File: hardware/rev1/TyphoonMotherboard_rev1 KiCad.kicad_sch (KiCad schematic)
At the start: 74 parts, among them J1 Conn_02x04_Odd_Even, J2 Conn_01x04_Pin, J3 UJ20-C-H-C-4-SMT-TR, J5 Conn_01x02_Pin, J6 Conn_01x02_Pin, J7 Conn_01x04_Pin, SW1 SW_Push, SW2 SW_Push, SW3 SW_Push, U1 USBLC6-2SC6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

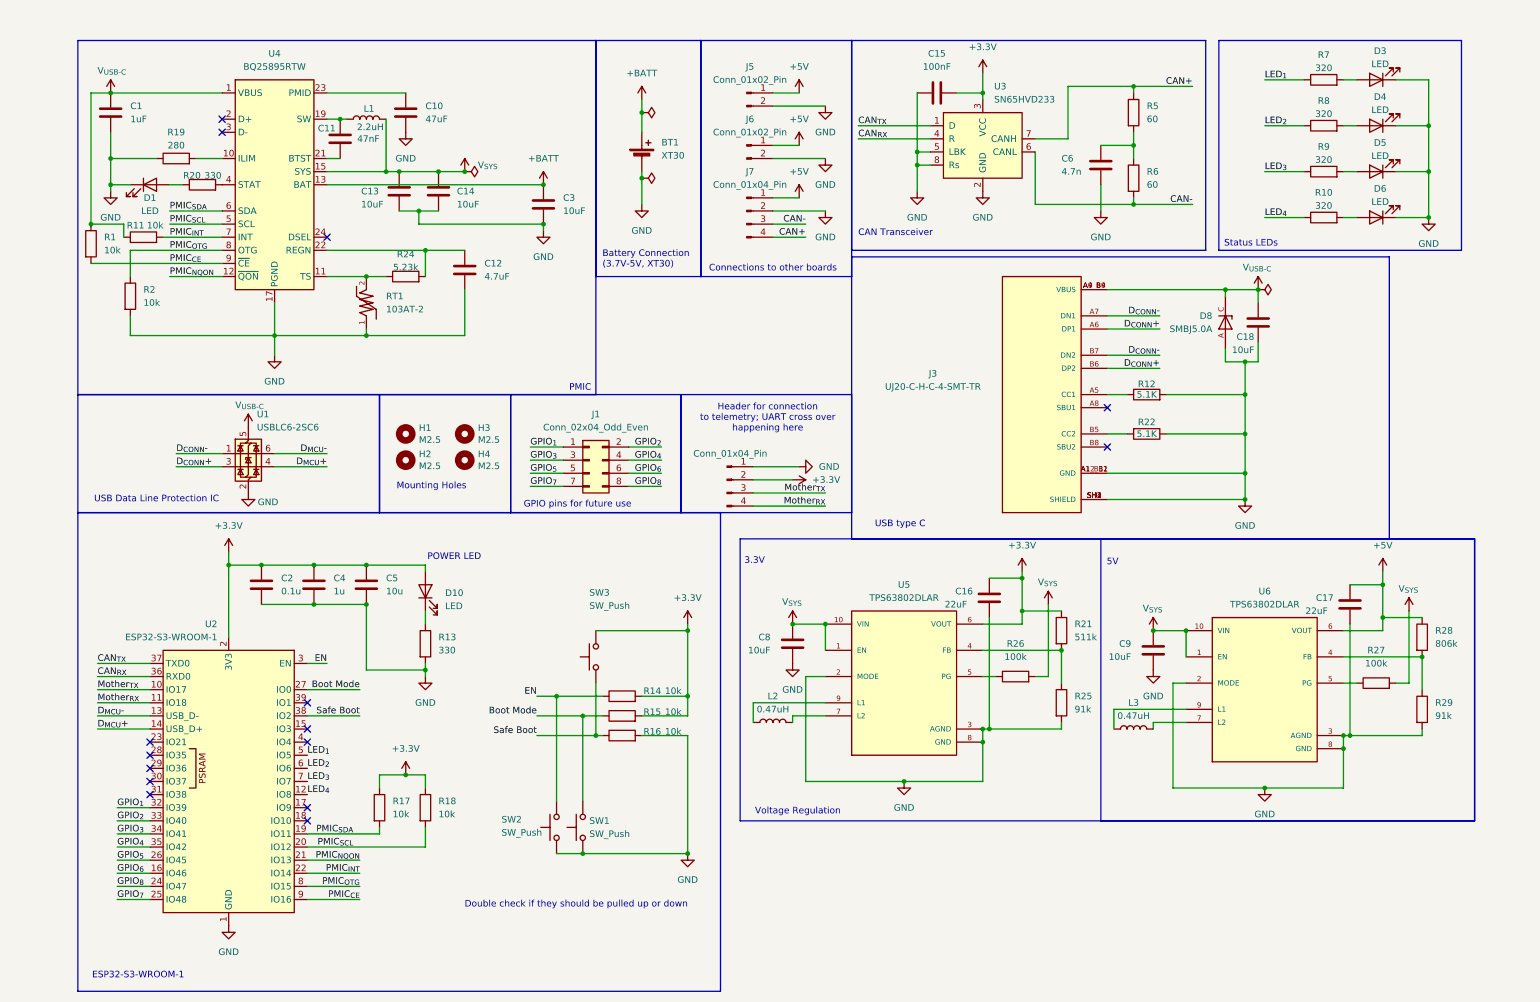
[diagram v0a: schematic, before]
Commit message: Updated the Symbol Fields for Motherboard
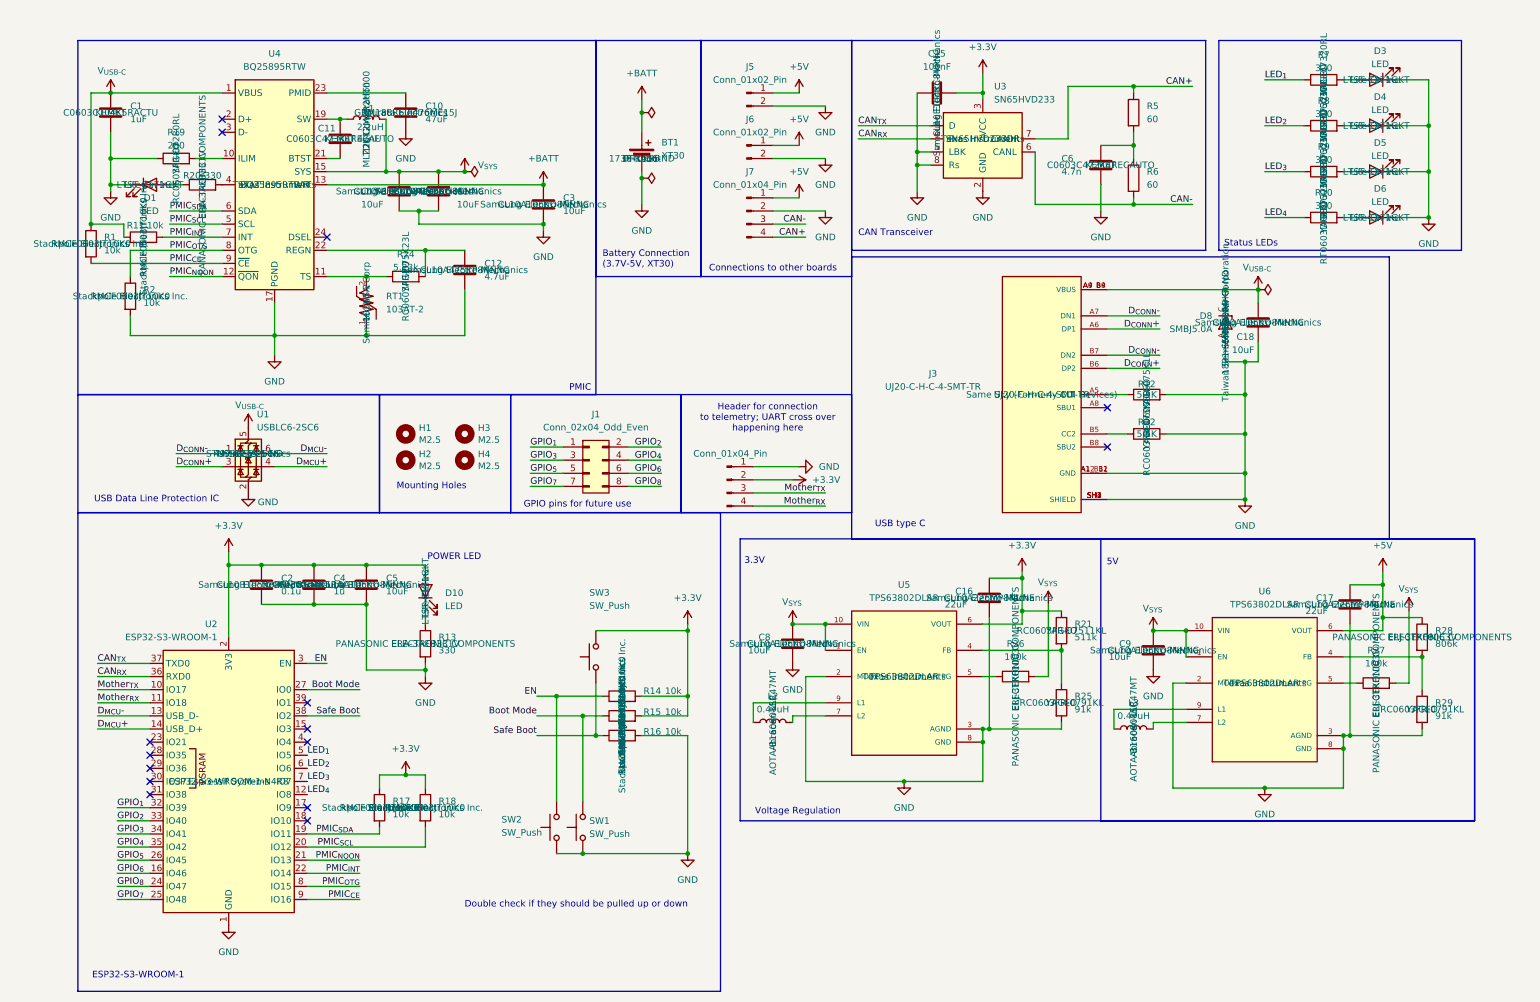
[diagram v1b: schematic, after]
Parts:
- BT1: Digikey Part Number (none) -> 1738-1436-ND; Manufacturer (none) -> DFRobot; Manufacturer Part Number (none) -> FIT0586
- C1, C4: Manufacturer (none) -> KEMET; Manufacturer Part Number (none) -> C0603C104K5RACTU
- C10: Manufacturer (none) -> Murata Electronics; Manufacturer Part Number (none) -> GRM188R60J476ME15J
- C11: Manufacturer (none) -> KEMET; Manufacturer Part Number (none) -> C0603C473K4RECAUTO
- C12: Manufacturer (none) -> Samsung Electro-Mechanics; Manufacturer Part Number (none) -> CL10A475KP8NNNC
- C13, C14, C18, C3, C8, C9: Manufacturer (none) -> Samsung Electro-Mechanics; Manufacturer Part Number (none) -> CL10A106KQ8NNNC
- C15: Manufacturer (none) -> Samsung Electro-Mechanics; Manufacturer Part Number (none) -> CL10E104KC8VPNC
- C16, C17: Manufacturer (none) -> Samsung Electro-Mechanics; Manufacturer Part Number (none) -> CL10A226MP8NUNE
- C2: Manufacturer (none) -> Samsung Electro-Mechanics; Manufacturer Part Number (none) -> CL10B105KP8NNNC
- C5: value 10u -> 10uF; Manufacturer (none) -> Samsung Electro-Mechanics; Manufacturer Part Number (none) -> CL10A106KQ8NNNC
- C6: Manufacturer (none) -> KEMET; Manufacturer Part Number (none) -> C0603C472K4RECAUTO
- D1, D10, D3, D4, D5, D6: Manufacturer (none) -> Lite-On Inc.; Manufacturer Part Number (none) -> LTST-C171GKT
- D8: Digikey Part Number (none) -> 1801-SMBJ5.0ADKR-ND; Manufacturer (none) -> Taiwan Semiconductor Corporation; Manufacturer Part Number (none) -> SMBJ5.0A
- J3: Manufacturer (none) -> Same Sky (Formerly CUI Devices); Manufacturer Part Number (none) -> UJ20-C-H-C-4-SMT-TR
- L1: Manufacturer (none) -> TDK Corporation; Manufacturer Part Number (none) -> MLZ2012M2R2HT000
- L2, L3: Manufacturer (none) -> Abracon LLC; Manufacturer Part Number (none) -> AOTA-B160808SR47MT
- R1, R11, R14, R15, R16, R17, R18, R2: Manufacturer (none) -> Stackpole Electronics Inc.; Manufacturer Part Number (none) -> RMCF0603JT10K0
- R10, R7, R8, R9: Manufacturer (none) -> YAGEO; Manufacturer Part Number (none) -> RT0603DRE07320RL
- R12, R22: Manufacturer (none) -> YAGEO; Manufacturer Part Number (none) -> RC0603FR-075K1L
- R13, R20: Manufacturer (none) -> PANASONIC ELECTRONIC COMPONENTS; Manufacturer Part Number (none) -> ERA-3AEB331V
- R19: Manufacturer (none) -> YAGEO; Manufacturer Part Number (none) -> RC0603FR-07280RL
- R21: Manufacturer (none) -> YAGEO; Manufacturer Part Number (none) -> RC0603FR-07511KL
- R24: Manufacturer (none) -> YAGEO; Manufacturer Part Number (none) -> RC0603FR-075K23L
- R25, R29: Manufacturer (none) -> YAGEO; Manufacturer Part Number (none) -> RC0603FR-0791KL
- R26, R27: Manufacturer (none) -> PANASONIC ELECTRONIC COMPONENTS; Manufacturer Part Number (none) -> ERJ-3EKF1003V
- R28: Manufacturer (none) -> PANASONIC ELECTRONIC COMPONENTS; Manufacturer Part Number (none) -> ERJ-3EKF8063V
- RT1: Manufacturer (none) -> Semitec USA Corp; Manufacturer Part Number (none) -> 103AT-2
- U1: Digikey Part Number (none) -> 497-5235-1-ND; Manufacturer (none) -> STMicroelectronics; Manufacturer Part Number (none) -> USBLC6-2SC6
- U2: Manufacturer (none) -> Espressif Systems; Manufacturer Part Number (none) -> ESP32-S3-WROOM-1-N4R8
- U3: Manufacturer (none) -> Texas Instruments; Manufacturer Part Number (none) -> SN65HVD233DR
- U4: Manufacturer (none) -> Texas Instruments; Manufacturer Part Number (none) -> BQ25895RTWR
- U5, U6: Manufacturer (none) -> Texas Instruments; Manufacturer Part Number (none) -> TPS63802DLAR
